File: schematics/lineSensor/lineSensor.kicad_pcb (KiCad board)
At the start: 2 copper layers, 27 parts, among them P1 CONN_01X01, P2 CONN_01X01, P3 CONN_01X01, P4 CONN_01X01, P5 CONN_01X01, P6 CONN_01X01, P7 CONN_01X01

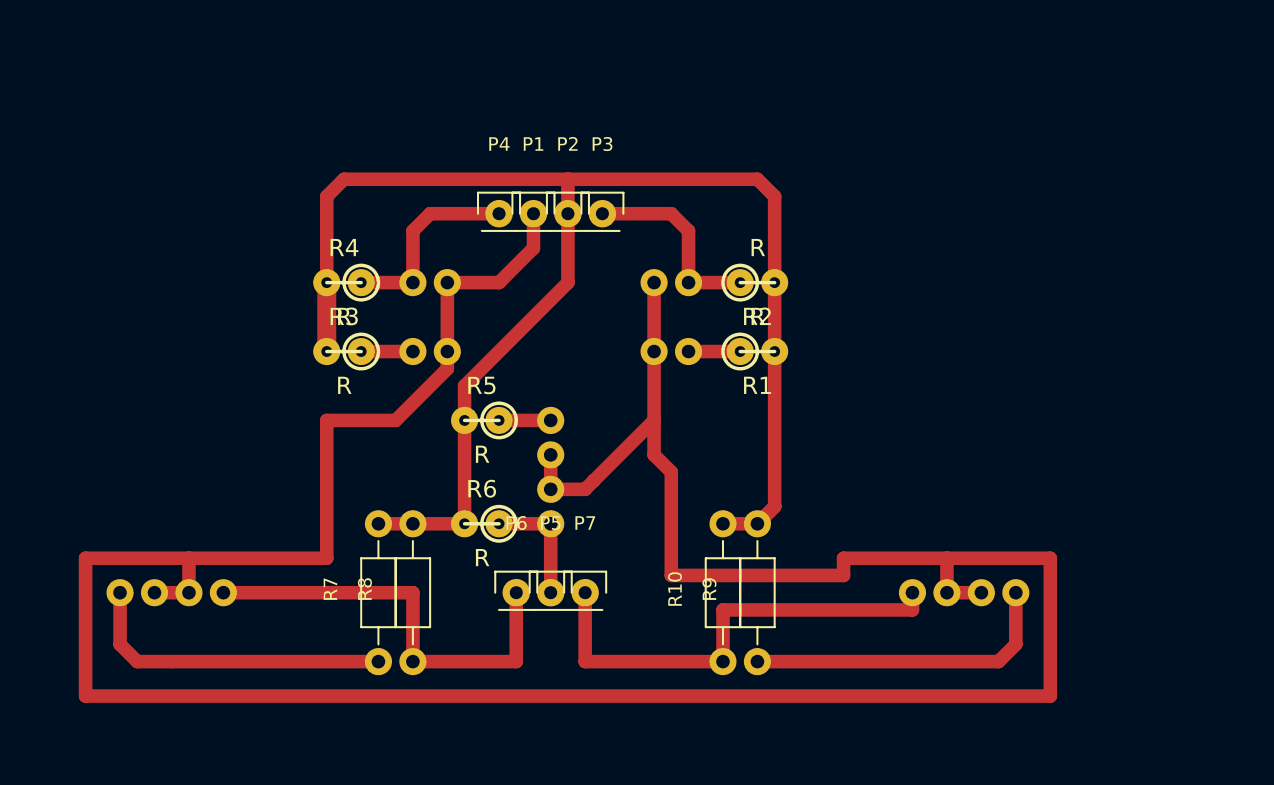
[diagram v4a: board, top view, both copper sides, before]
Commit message: Rewrite lineSensors scheme and small update bug
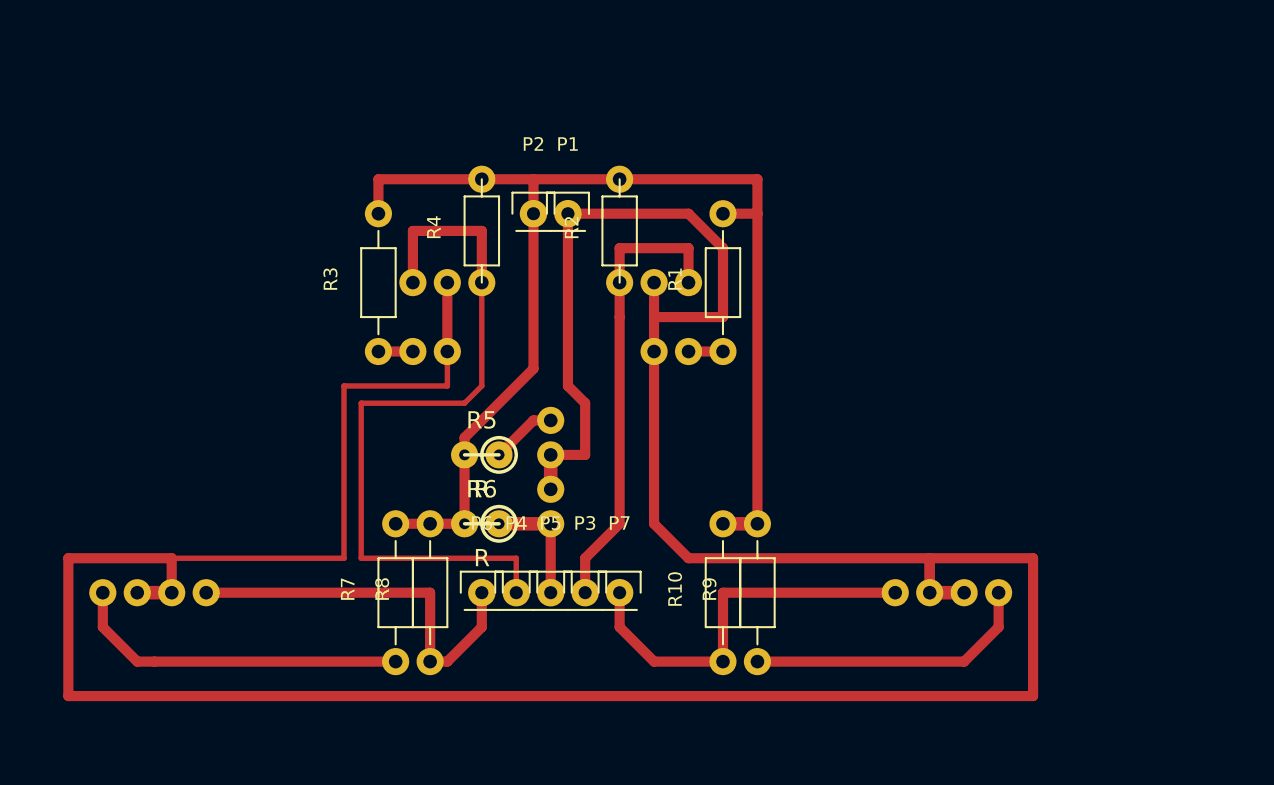
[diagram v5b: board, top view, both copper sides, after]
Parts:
- R1, R2, R3, R4: footprint w_pth_resistors:rc05_vert -> Resistors_ThroughHole:Resistor_Horizontal_RM10mm
- moved P3 28.0 mm to (149.9, 129.5)
- moved P4 28.0 mm to (144.8, 129.5)
- moved R2 10.2 mm to (152.4, 108.0), turned to 90 degrees
- moved R4 10.2 mm to (142.2, 108.0), turned to 90 degrees
- moved P1 2.54 mm to (148.6, 101.6)
- moved P2 2.54 mm to (146.1, 101.6)
- moved P6 2.54 mm to (142.2, 129.5)
- moved P7 2.54 mm to (152.4, 129.5)
- moved R1 2.54 mm to (160.0, 111.8), turned to 90 degrees
- moved R3 2.54 mm to (134.6, 111.8), turned to 90 degrees
- moved R5 2.54 mm to (142.2, 119.4)
- moved D10 1.27 mm to (172.7, 129.5)
- moved D9 1.27 mm to (180.3, 129.5)
- moved R8 1.27 mm to (138.4, 134.6)
- moved D7 1.27 mm to (114.3, 129.5)
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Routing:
- net Net-(D4-Pad1): track 14.5 -> 55.1 mm
- net Net-(D1-Pad2): track 219.9 -> 245.2 mm
- net Net-(D2-Pad1): track 14.5 -> 34.1 mm
- net Net-(P2-Pad1): track 109.4 -> 93.5 mm
- net Net-(D10-Pad1): track 34.3 -> 29.0 mm
- net Net-(D8-Pad1): track 31.8 -> 29.0 mm
- net Net-(D9-Pad1): track 23.4 -> 21.4 mm
- net Net-(D7-Pad1): track 23.4 -> 25.2 mm
- net Net-(D3-Pad1): track 3.81 -> 2.54 mm
- net Net-(D1-Pad1): track 3.81 -> 2.54 mm
- net Net-(D5-Pad1): track 3.81 -> 4.86 mm

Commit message: Update schematic
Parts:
- R5, R6: footprint w_pth_resistors:rc05_vert -> w_pth_resistors:RC03
- moved R6 3.59 mm to (139.7, 121.9)
- moved R5 2.84 mm to (139.7, 118.1)
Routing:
- net Net-(P2-Pad1): track 93.5 -> 95.7 mm
- net Net-(D6-Pad1): track 8.89 -> 10.7 mm
- net Net-(D5-Pad1): track 4.86 -> 4.34 mm
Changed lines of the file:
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@@
     (thickness 1.6)
     (drawings 7)
-    (tracks 85)
+    (tracks 88)
     (zones 0)
     (modules 27)
@@
   )
   (setup
-    (last_trace_width 0.4)
+    (last_trace_width 0.75)
     (user_trace_width 0.4)
     (user_trace_width 0.75)
@@
     )
   )
-  (module w_pth_resistors:rc05_vert (layer F.Cu)
-    (at 142.24 124.46 180)
-    (descr "Resistor, RC05 vertical")
-    (fp_text reference R6 (at 0 2.54 180) (layer F.SilkS)
-      (effects (font (thickness 0.3048)))
-    )
-    (fp_text value R (at 0 -2.54 180) (layer F.SilkS)
-      (effects (font (thickness 0.3048)))
-    )
-    (fp_line (start -1.27 0) (end 1.27 0) (layer F.SilkS) (width 0.254))
-    (fp_circle (center -1.27 0) (end 0 0) (layer F.SilkS) (width 0.254))
-    (pad 1 thru_hole circle (at -1.27 0 180) (size 1.99898 1.99898) (drill 0.8001) (layers *.Cu *.Mask F.SilkS)
-      (net 7 "Net-(D6-Pad1)"))
-    (pad 2 thru_hole circle (at 1.27 0 180) (size 1.99898 1.99898) (drill 0.8001) (layers *.Cu *.Mask F.SilkS)
-      (net 12 "Net-(P2-Pad1)"))
-    (model walter/pth_resistors/rc05vert.wrl
-      (at (xyz 0 0 0))
-      (scale (xyz 1 1 1))
-      (rotate (xyz 0 0 0))
-    )
-  )
-  (module w_pth_resistors:rc05_vert (layer F.Cu)
-    (at 142.24 119.38 180)
-    (descr "Resistor, RC05 vertical")
-    (fp_text reference R5 (at 0 2.54 180) (layer F.SilkS)
-      (effects (font (thickness 0.3048)))
-    )
-    (fp_text value R (at 0 -2.54 180) (layer F.SilkS)
-      (effects (font (thickness 0.3048)))
-    )
-    (fp_line (start -1.27 0) (end 1.27 0) (layer F.SilkS) (width 0.254))
-    (fp_circle (center -1.27 0) (end 0 0) (layer F.SilkS) (width 0.254))
-    (pad 1 thru_hole circle (at -1.27 0 180) (size 1.99898 1.99898) (drill 0.8001) (layers *.Cu *.Mask F.SilkS)
-      (net 6 "Net-(D5-Pad1)"))
-    (pad 2 thru_hole circle (at 1.27 0 180) (size 1.99898 1.99898) (drill 0.8001) (layers *.Cu *.Mask F.SilkS)
-      (net 12 "Net-(P2-Pad1)"))
-    (model walter/pth_resistors/rc05vert.wrl
-      (at (xyz 0 0 0))
-      (scale (xyz 1 1 1))
-      (rotate (xyz 0 0 0))
-    )
-  )
   (module Resistors_ThroughHole:Resistor_Horizontal_RM10mm (layer F.Cu)
     (at 134.62 111.76 90)
@@
     )
   )
+  (module w_pth_resistors:RC03 (layer F.Cu)
+    (at 139.7 118.11 180)
+    (descr "Resistor, RC03")
+    (tags R)
+    (autoplace_cost180 10)
+    (fp_text reference R5 (at 0 0 180) (layer F.SilkS)
+      (effects (font (size 1.397 1.27) (thickness 0.2032)))
+    )
+    (fp_text value R (at 0 2.032 180) (layer F.SilkS) hide
+      (effects (font (size 1.397 1.27) (thickness 0.2032)))
+    )
+    (fp_line (start 2.159 0) (end 3.81 0) (layer F.SilkS) (width 0.254))
+    (fp_line (start -2.159 0) (end -3.81 0) (layer F.SilkS) (width 0.254))
+    (fp_line (start -2.159 -0.889) (end -2.159 0.889) (layer F.SilkS) (width 0.254))
+    (fp_line (start -2.159 0.889) (end 2.159 0.889) (layer F.SilkS) (width 0.254))
+    (fp_line (start 2.159 0.889) (end 2.159 -0.889) (layer F.SilkS) (width 0.254))
+    (fp_line (start 2.159 -0.889) (end -2.159 -0.889) (layer F.SilkS) (width 0.254))
+    (pad 1 thru_hole circle (at -3.81 0 180) (size 1.99898 1.99898) (drill 0.8001) (layers *.Cu *.Mask F.SilkS)
+      (net 6 "Net-(D5-Pad1)"))
+    (pad 2 thru_hole circle (at 3.81 0 180) (size 1.99898 1.99898) (drill 0.8001) (layers *.Cu *.Mask F.SilkS)
+      (net 12 "Net-(P2-Pad1)"))
+    (model walter/pth_resistors/rc03.wrl
+      (at (xyz 0 0 0))
+      (scale (xyz 1 1 1))
+      (rotate (xyz 0 0 0))
+    )
+  )
+  (module w_pth_resistors:RC03 (layer F.Cu)
+    (at 139.7 121.92 180)
+    (descr "Resistor, RC03")
+    (tags R)
+    (autoplace_cost180 10)
+    (fp_text reference R6 (at 0 0 180) (layer F.SilkS)
+      (effects (font (size 1.397 1.27) (thickness 0.2032)))
+    )
+    (fp_text value R (at 0 2.032 180) (layer F.SilkS) hide
+      (effects (font (size 1.397 1.27) (thickness 0.2032)))
+    )
+    (fp_line (start 2.159 0) (end 3.81 0) (layer F.SilkS) (width 0.254))
+    (fp_line (start -2.159 0) (end -3.81 0) (layer F.SilkS) (width 0.254))
+    (fp_line (start -2.159 -0.889) (end -2.159 0.889) (layer F.SilkS) (width 0.254))
+    (fp_line (start -2.159 0.889) (end 2.159 0.889) (layer F.SilkS) (width 0.254))
+    (fp_line (start 2.159 0.889) (end 2.159 -0.889) (layer F.SilkS) (width 0.254))
+    (fp_line (start 2.159 -0.889) (end -2.159 -0.889) (layer F.SilkS) (width 0.254))
+    (pad 1 thru_hole circle (at -3.81 0 180) (size 1.99898 1.99898) (drill 0.8001) (layers *.Cu *.Mask F.SilkS)
+      (net 7 "Net-(D6-Pad1)"))
+    (pad 2 thru_hole circle (at 3.81 0 180) (size 1.99898 1.99898) (drill 0.8001) (layers *.Cu *.Mask F.SilkS)
+      (net 12 "Net-(P2-Pad1)"))
+    (model walter/pth_resistors/rc03.wrl
+      (at (xyz 0 0 0))
+      (scale (xyz 1 1 1))
+      (rotate (xyz 0 0 0))
+    )
+  )
   (gr_line (start 127 139.7) (end 185.42 139.7) (angle 90) (layer Eco1.User) (width 0.2))
   (gr_line (start 109.22 139.7) (end 127 139.7) (angle 90) (layer Eco1.User) (width 0.2))
@@
   (gr_line (start 109.22 33.02) (end 185.42 33.02) (angle 90) (layer Eco1.User) (width 0.2))
   (segment (start 160.02 111.76) (end 157.48 111.76) (width 0.75) (layer F.Cu) (net 1))
-  (segment (start 139.7 111.76) (end 139.7 114.3) (width 0.4) (layer F.Cu) (net 2) (status 400000))
+  (segment (start 139.7 111.76) (end 139.7 114.3) (width 0.4) (layer F.Cu) (net 2))
   (segment (start 132.08 127) (end 119.38 127) (width 0.4) (layer F.Cu) (net 2))
   (segment (start 132.08 114.3) (end 132.08 127) (width 0.4) (layer F.Cu) (net 2))
@@
   (segment (start 152.4 109.22) (end 152.4 124.46) (width 0.75) (layer F.Cu) (net 3))
   (segment (start 134.62 111.76) (end 137.16 111.76) (width 0.75) (layer F.Cu) (net 4))
-  (segment (start 144.78 129.54) (end 144.78 127) (width 0.4) (layer F.Cu) (net 5) (status 400000))
-  (segment (start 142.24 114.3) (end 142.24 106.68) (width 0.4) (layer F.Cu) (net 5) (status 800000))
+  (segment (start 144.78 129.54) (end 144.78 127) (width 0.4) (layer F.Cu) (net 5))
+  (segment (start 142.24 114.3) (end 142.24 106.68) (width 0.4) (layer F.Cu) (net 5))
   (segment (start 140.97 115.57) (end 142.24 114.3) (width 0.4) (layer F.Cu) (net 5))
   (segment (start 133.35 115.57) (end 140.97 115.57) (width 0.4) (layer F.Cu) (net 5))
@@
   (segment (start 137.16 102.87) (end 137.16 106.68) (width 0.75) (layer F.Cu) (net 5))
   (segment (start 142.24 102.87) (end 137.16 102.87) (width 0.75) (layer F.Cu) (net 5))
-  (segment (start 147.32 116.84) (end 146.05 116.84) (width 0.75) (layer F.Cu) (net 6))
-  (segment (start 146.05 116.84) (end 143.51 119.38) (width 0.75) (layer F.Cu) (net 6))
+  (segment (start 143.51 118.11) (end 144.78 116.84) (width 0.75) (layer F.Cu) (net 6) (status 400000))
+  (segment (start 144.78 116.84) (end 147.32 116.84) (width 0.75) (layer F.Cu) (net 6) (status 800000))
+  (segment (start 143.51 121.92) (end 143.51 123.19) (width 0.75) (layer F.Cu) (net 7) (status 400000))
+  (segment (start 144.78 124.46) (end 147.32 124.46) (width 0.75) (layer F.Cu) (net 7) (status 800000))
+  (segment (start 143.51 123.19) (end 144.78 124.46) (width 0.75) (layer F.Cu) (net 7))
   (segment (start 147.32 129.54) (end 147.32 124.46) (width 0.75) (layer F.Cu) (net 7))
-  (segment (start 147.32 124.46) (end 143.51 124.46) (width 1) (layer F.Cu) (net 7))
   (segment (start 116.84 134.62) (end 118.11 134.62) (width 0.75) (layer F.Cu) (net 8))
   (segment (start 116.84 134.62) (end 114.3 132.08) (width 0.75) (layer F.Cu) (net 8))
@@
   (segment (start 154.94 134.62) (end 160.02 134.62) (width 0.75) (layer F.Cu) (net 11))
   (segment (start 152.4 132.08) (end 154.94 134.62) (width 0.75) (layer F.Cu) (net 11))
+  (segment (start 135.89 121.92) (end 135.89 124.46) (width 0.75) (layer F.Cu) (net 12) (status C00000))
+  (segment (start 135.89 118.11) (end 140.335 118.11) (width 0.4) (layer F.Cu) (net 12) (status 400000))
+  (segment (start 146.05 112.395) (end 146.05 101.6) (width 0.4) (layer F.Cu) (net 12) (status 800000))
+  (segment (start 144.78 113.665) (end 146.05 112.395) (width 0.4) (layer F.Cu) (net 12))
+  (segment (start 140.335 118.11) (end 144.78 113.665) (width 0.4) (layer F.Cu) (net 12))
+  (segment (start 135.89 121.92) (end 135.89 118.11) (width 0.75) (layer F.Cu) (net 12) (status C00000))
   (segment (start 142.24 99.06) (end 134.62 99.06) (width 0.75) (layer F.Cu) (net 12))
   (segment (start 134.62 99.06) (end 134.62 101.6) (width 0.75) (layer F.Cu) (net 12))
-  (segment (start 138.43 124.46) (end 140.97 124.46) (width 0.75) (layer F.Cu) (net 12))
   (segment (start 162.56 101.6) (end 162.56 99.06) (width 0.75) (layer F.Cu) (net 12))
   (segment (start 162.56 99.06) (end 152.4 99.06) (width 0.75) (layer F.Cu) (net 12))
@@
   (segment (start 152.4 99.06) (end 146.05 99.06) (width 0.75) (layer F.Cu) (net 12))
   (segment (start 146.05 99.06) (end 142.24 99.06) (width 0.75) (layer F.Cu) (net 12))
-  (segment (start 140.97 119.38) (end 140.97 118.11) (width 0.75) (layer F.Cu) (net 12))
-  (segment (start 146.05 113.03) (end 146.05 101.6) (width 0.75) (layer F.Cu) (net 12))
-  (segment (start 140.97 118.11) (end 146.05 113.03) (width 0.75) (layer F.Cu) (net 12))
   (segment (start 135.89 124.46) (end 138.43 124.46) (width 0.75) (layer F.Cu) (net 12))
-  (segment (start 140.97 119.38) (end 140.97 124.46) (width 0.75) (layer F.Cu) (net 12))
   (segment (start 162.56 124.46) (end 160.02 124.46) (width 1) (layer F.Cu) (net 12))
 )

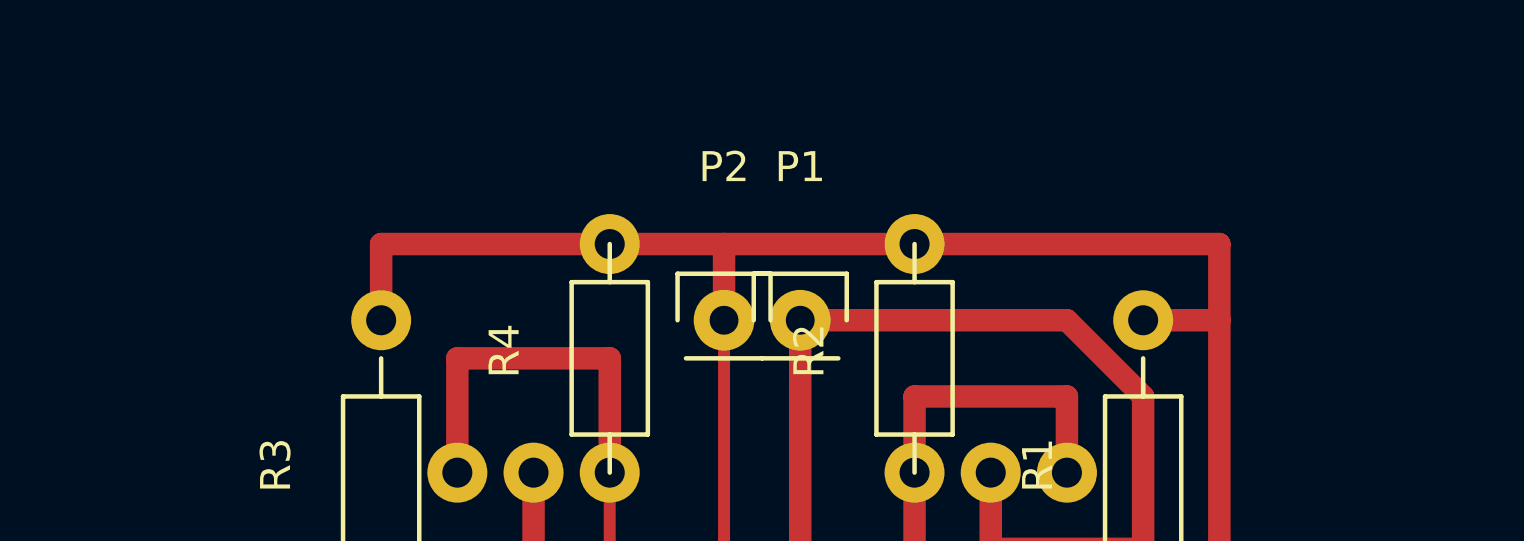
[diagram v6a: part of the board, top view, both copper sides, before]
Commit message: Update schematics for whiskers
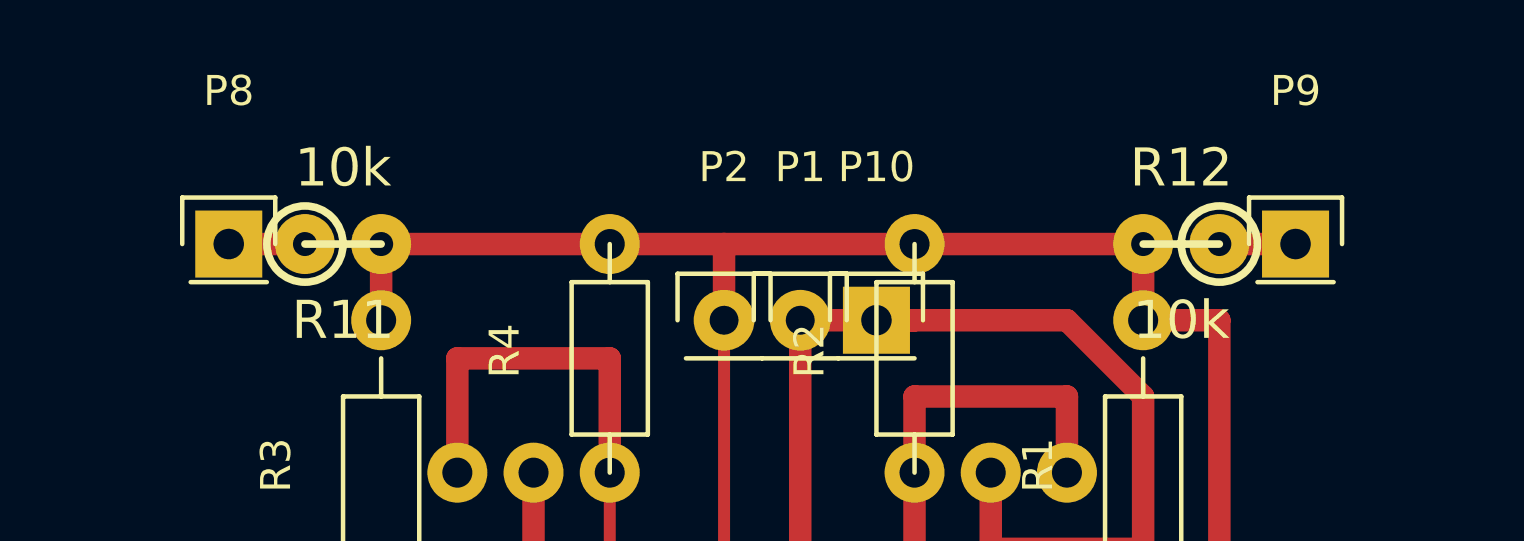
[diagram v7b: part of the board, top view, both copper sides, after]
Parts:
- added P10: CONN_01X01, Pin_Headers:Pin_Header_Straight_1x01, F.Cu at (151.1, 101.6)
- added P8: CONN_01X01, Pin_Headers:Pin_Header_Straight_1x01, F.Cu at (129.5, 99.1)
- added P9: CONN_01X01, Pin_Headers:Pin_Header_Straight_1x01, F.Cu at (165.1, 99.1)
- added R11: 10k, w_pth_resistors:rc05_vert, F.Cu at (133.3, 99.1)
- added R12: 10k, w_pth_resistors:rc05_vert, F.Cu at (161.3, 99.1)
- R1, R3, R5, R7, R9: value R -> 150
- R10, R2, R4, R6, R8: value R -> 510k
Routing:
- net Net-(P8-Pad1): track 0.00 -> 2.54 mm
- net Net-(P9-Pad1): track 0.00 -> 2.54 mm
- net Net-(P2-Pad1): track 95.7 -> 93.2 mm
- net Net-(D1-Pad2): track 245.2 -> 246.5 mm

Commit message: SCHEMATICS: prepare Lighthouse for production
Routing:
- net Net-(P2-Pad1): track 93.2 -> 109.7 mm
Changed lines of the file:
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@@
     (thickness 1.6)
     (drawings 7)
-    (tracks 92)
+    (tracks 95)
     (zones 0)
     (modules 32)
@@
   (gr_line (start 109.22 33.02) (end 185.42 33.02) (angle 90) (layer Eco1.User) (width 0.2))
   (segment (start 160.02 111.76) (end 157.48 111.76) (width 0.75) (layer F.Cu) (net 1))
+  (segment (start 119.38 127) (end 132.08 127) (width 0.75) (layer F.Cu) (net 2))
+  (segment (start 139.7 114.3) (end 132.08 114.3) (width 0.4) (layer F.Cu) (net 2))
+  (segment (start 132.08 114.3) (end 132.08 127) (width 0.4) (layer F.Cu) (net 2))
+  (segment (start 139.7 111.76) (end 139.7 114.3) (width 0.4) (layer F.Cu) (net 2))
   (segment (start 151.13 101.6) (end 152.4 101.6) (width 0.75) (layer F.Cu) (net 2))
-  (segment (start 139.7 111.76) (end 139.7 114.3) (width 0.4) (layer F.Cu) (net 2))
-  (segment (start 132.08 127) (end 119.38 127) (width 0.4) (layer F.Cu) (net 2))
-  (segment (start 132.08 114.3) (end 132.08 127) (width 0.4) (layer F.Cu) (net 2))
-  (segment (start 139.7 114.3) (end 132.08 114.3) (width 0.4) (layer F.Cu) (net 2))
   (segment (start 154.94 111.76) (end 154.94 124.46) (width 0.75) (layer F.Cu) (net 2))
   (segment (start 157.48 127) (end 175.26 127) (width 0.75) (layer F.Cu) (net 2))
@@
   (segment (start 152.4 109.22) (end 152.4 124.46) (width 0.75) (layer F.Cu) (net 3))
   (segment (start 134.62 111.76) (end 137.16 111.76) (width 0.75) (layer F.Cu) (net 4))
-  (segment (start 144.78 129.54) (end 144.78 127) (width 0.4) (layer F.Cu) (net 5))
+  (segment (start 144.78 127) (end 144.78 129.54) (width 0.75) (layer F.Cu) (net 5) (status 800000))
+  (segment (start 134.62 127) (end 144.78 127) (width 0.75) (layer F.Cu) (net 5))
   (segment (start 142.24 114.3) (end 142.24 106.68) (width 0.4) (layer F.Cu) (net 5))
   (segment (start 140.97 115.57) (end 142.24 114.3) (width 0.4) (layer F.Cu) (net 5))
   (segment (start 133.35 115.57) (end 140.97 115.57) (width 0.4) (layer F.Cu) (net 5))
   (segment (start 133.35 127) (end 133.35 115.57) (width 0.4) (layer F.Cu) (net 5))
-  (segment (start 144.78 127) (end 133.35 127) (width 0.4) (layer F.Cu) (net 5))
+  (segment (start 134.62 127) (end 133.35 127) (width 0.4) (layer F.Cu) (net 5))
   (segment (start 142.24 106.68) (end 142.24 102.87) (width 0.75) (layer F.Cu) (net 5))
   (segment (start 137.16 102.87) (end 137.16 106.68) (width 0.75) (layer F.Cu) (net 5))
@@
   (segment (start 154.94 134.62) (end 160.02 134.62) (width 0.75) (layer F.Cu) (net 11))
   (segment (start 152.4 132.08) (end 154.94 134.62) (width 0.75) (layer F.Cu) (net 11))
-  (segment (start 160.02 101.6) (end 160.02 99.06) (width 0.75) (layer F.Cu) (net 12) (status C00000))
+  (segment (start 146.05 101.6) (end 146.05 113.03) (width 0.75) (layer F.Cu) (net 12) (status 400000))
+  (segment (start 135.89 118.11) (end 140.97 118.11) (width 0.75) (layer F.Cu) (net 12) (status 400000))
+  (segment (start 160.02 101.6) (end 160.02 99.06) (width 0.75) (layer F.Cu) (net 12))
   (segment (start 160.02 99.06) (end 152.4 99.06) (width 0.75) (layer F.Cu) (net 12))
   (segment (start 134.62 99.06) (end 134.62 101.6) (width 0.75) (layer F.Cu) (net 12))
